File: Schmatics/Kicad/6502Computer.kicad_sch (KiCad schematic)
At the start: 8 parts

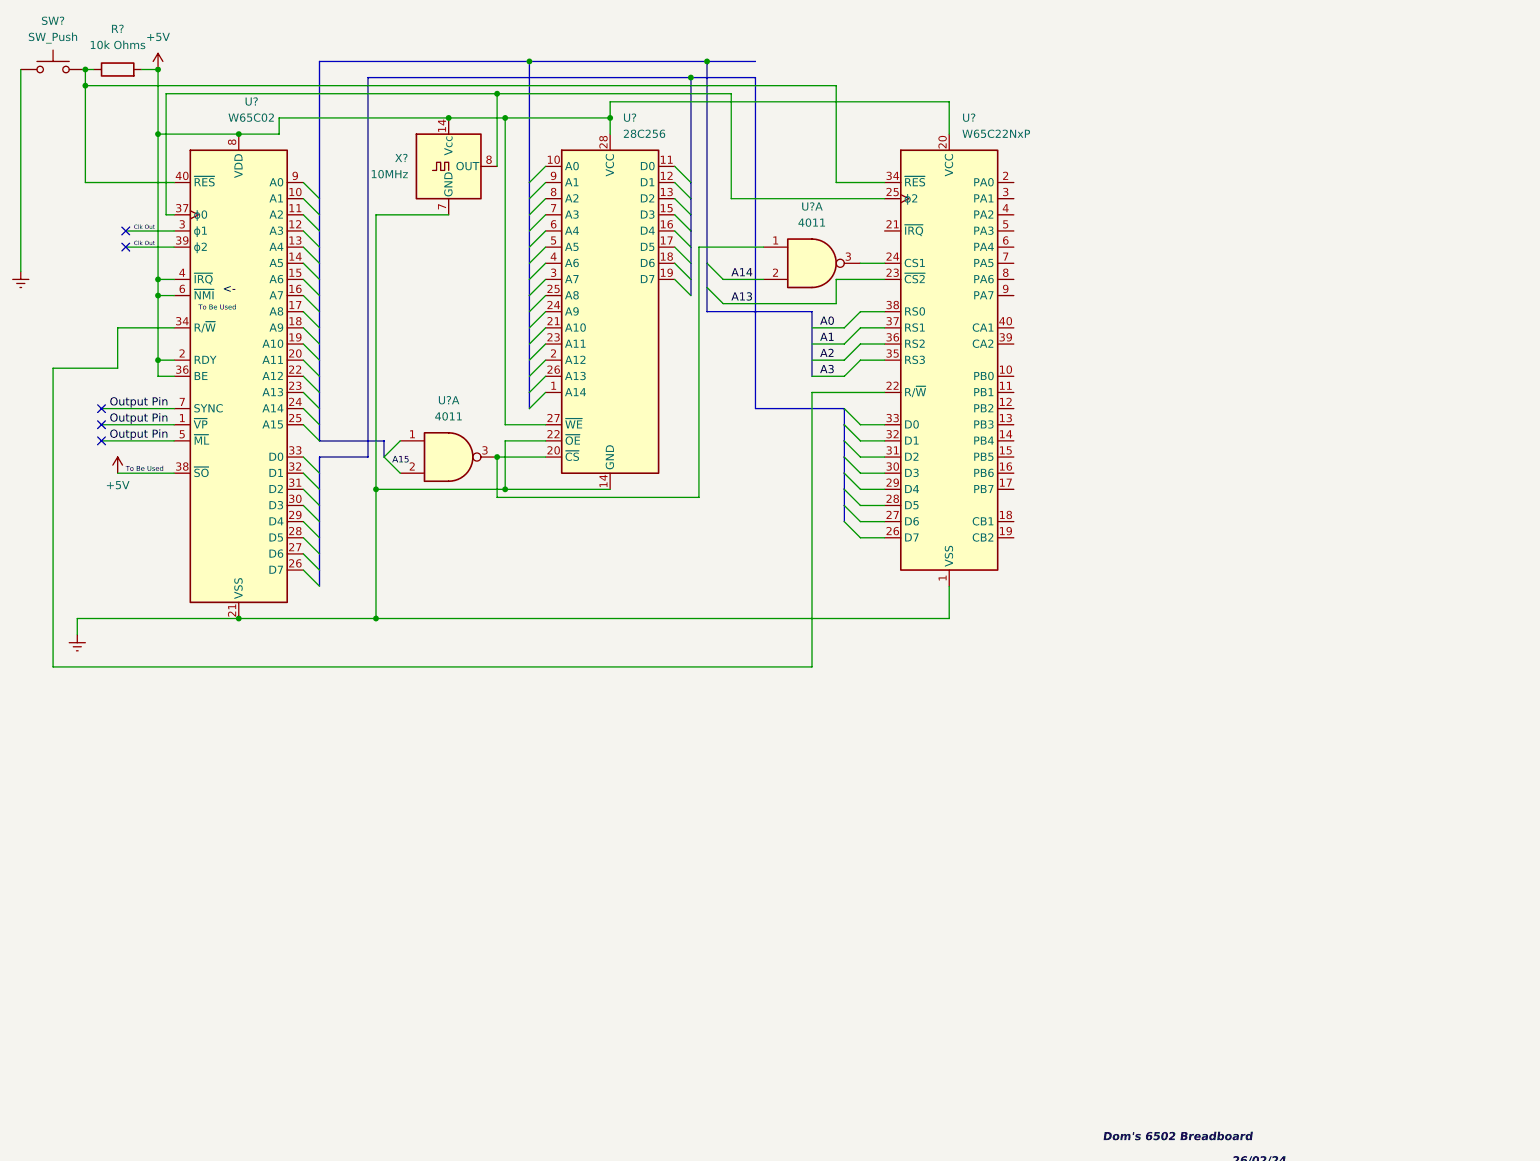
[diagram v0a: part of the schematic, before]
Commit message: Update schematic configuration and add new components
The schematic configuration was updated to include presets and detailed design settings. Two new elements, a trim-potentiometer and an LCD display, were also added to the PSI schematic. In addition, information about a new RAM memory HM62256BLP was added.
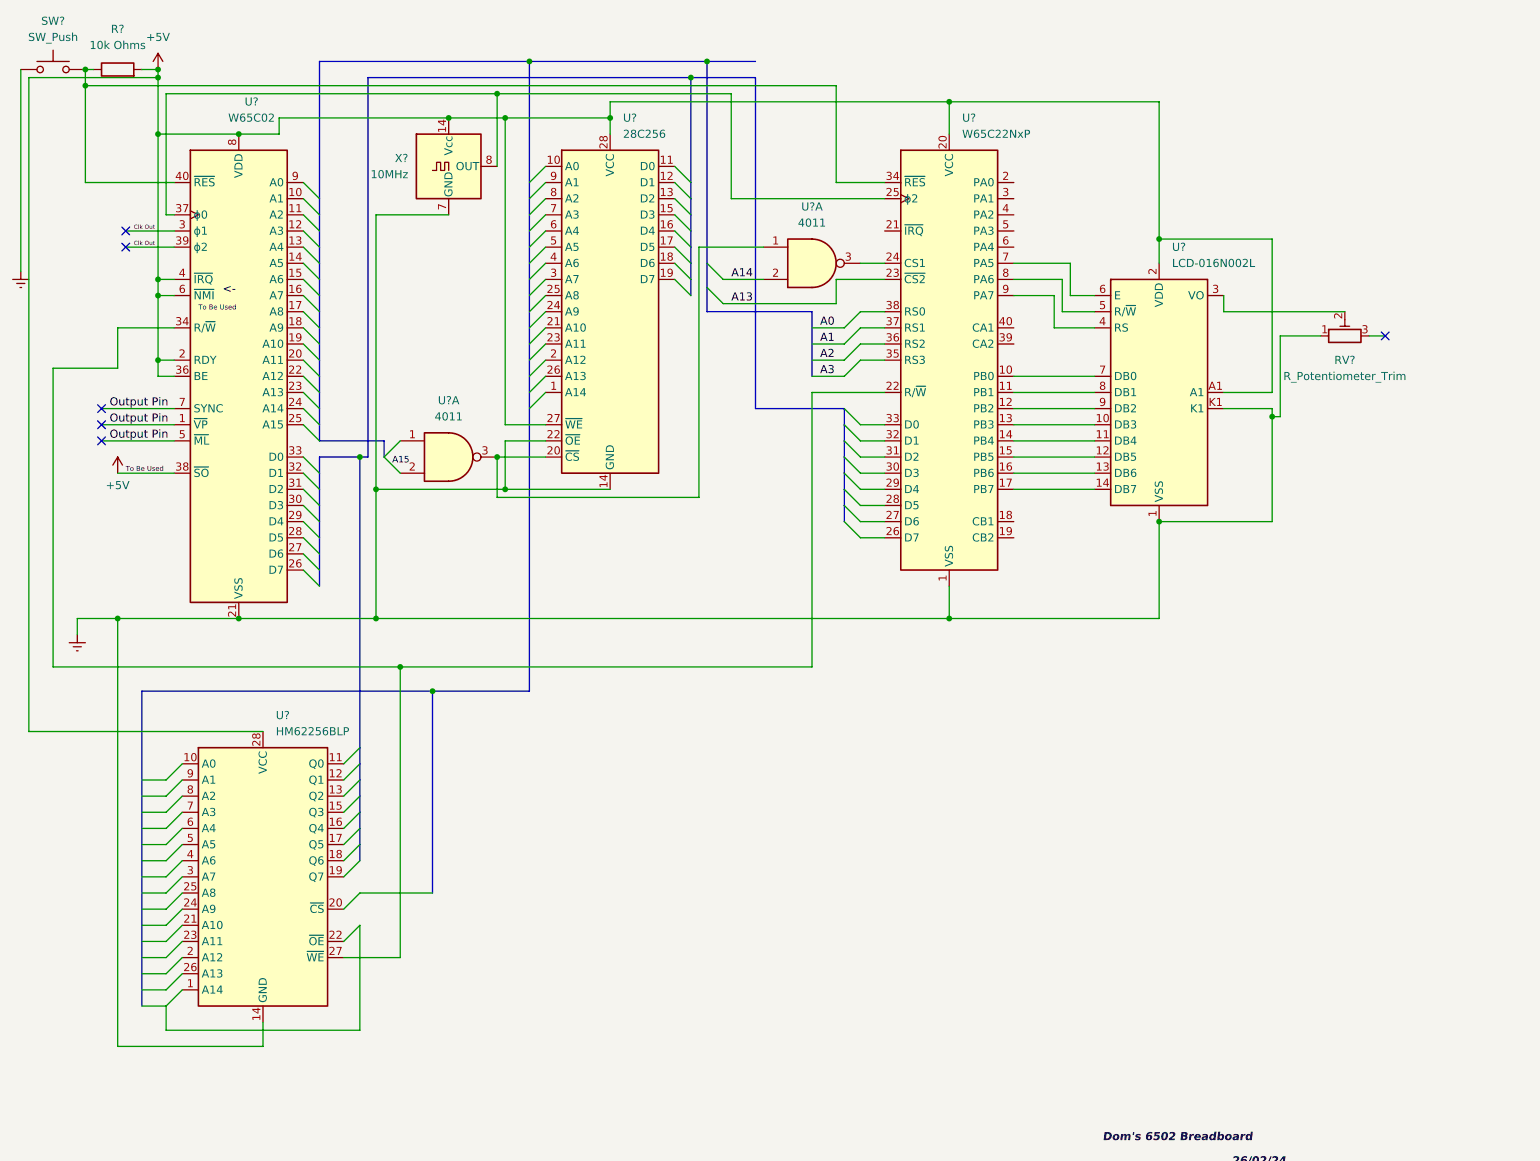
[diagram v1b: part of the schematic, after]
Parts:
- added RV?: R_Potentiometer_Trim, symbol Device:R_Potentiometer_Trim
- added U?: LCD-016N002L, Display:LCD-016N002L, symbol Display_Character:LCD-016N002L
- added U?: HM62256BLP, Package_DIP:DIP-28_W15.24mm, symbol Memory_RAM:HM62256BLP
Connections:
- net +5V: now also U?.2 (VDD), U?.28 (VCC), U?.A1
- net Earth: now also RV?.1, U?.1 (VSS), U?.14 (GND), U?.K1
- net at U?.10 (PB0): now also U?.7 (DB0)
- net at U?.11 (PB1): now also U?.8 (DB1)
- net at U?.12 (PB2): now also U?.9 (DB2)
- net at U?.13 (PB3): now also U?.10 (DB3)
- net at U?.14 (PB4): now also U?.11 (DB4)
- net at U?.15 (PB5): now also U?.12 (DB5)
- net at U?.16 (PB6): now also U?.13 (DB6)
- net at U?.17 (PB7): now also U?.14 (DB7)
- net at U?.22 (R/~{W}), U?.34 (R/~{W}): now also U?.27 (~{WE})
- net at U?.7 (PA5): now also U?.6 (E)
- net at U?.8 (PA6): now also U?.5 (R/~{W})
- net at U?.9 (PA7): now also U?.4 (RS)
- new net: RV?.2, U?.3 (VO)
- no-connect marks 5 -> 6

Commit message: Schemat
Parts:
- added C1, C2: 22pF, symbol Device:C
- added J1: Video Out, symbol Connector:Conn_Coaxial
- added R1: 470R, symbol Device:R
- added R2: 1K, symbol Device:R
- added R3: 10K, symbol Device:R
- added U1: 74HCT166, symbol 74xx:74HCT164
- added U2: ATmega328-P, Package_DIP:DIP-28_W7.62mm, symbol MCU_Microchip_ATmega:ATmega328-P
- added Y1: Crystal, symbol Device:Crystal
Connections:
- net A14 is gone; now on net A13: U?.2
- net +5V: now also U1.16 (VCC)
- net A13: now also R?.1, SW?.2, U?.34 (~{RES}), U?.40 (~{RES}), U1.9 (~{MR})
- net Earth: now also J1.2 (Ext), R3.2, U1.1 (DS), U1.6 (CE), U1.8 (GND), U2.20 (AVCC), U2.22 (GND), U2.7 (VCC), U2.8 (GND)
- new net: C1.1, U2.9 (XTAL1/PB6), Y1.2
- new net: C1.2, C2.2
- new net: R2.1, U2.14 (PB0)
- new net: J1.1 (In), R1.2, R2.2
- new net: C2.1, U1.7 (CP), U2.10 (XTAL2/PB7), Y1.1
- new net: R1.1, U1.13 (Q7)
- new net: U1.15 (PEB), U2.26 (PC3)
- new net PD7: R3.1

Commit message: Schemat
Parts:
- removed R?: 10k Ohms, symbol Device:R
- removed RV?: R_Potentiometer_Trim, symbol Device:R_Potentiometer_Trim
- removed U? (x2): 4011, symbol 4xxx:4011
- removed U?: W65C22NxP, Package_DIP:DIP-40_W15.24mm, symbol 6502:W65C22NxP
- removed U?: 28C256, symbol EEProm:28C256
- removed U?: LCD-016N002L, Display:LCD-016N002L, symbol Display_Character:LCD-016N002L
- removed U?: HM62256BLP, Package_DIP:DIP-28_W15.24mm, symbol Memory_RAM:HM62256BLP
- removed U?: W65C02, Package_DIP:DIP-40_W15.24mm, symbol 6502:W65C02SxP
- removed X?: 10MHz, Oscillator:Oscillator_DIP-14, symbol Oscillator:ACO-xxxMHz
- added C3, C4: 22pF, symbol Device:C
- added C5, C6, C7, C8: 0.1uf, symbol Device:C
- added J2: Keyboard + Video, symbol Connector:DE9_Plug
- added J3: PS/2 Keyboard, symbol Connector:Mini-DIN-6
- added R4, R5: 10K, symbol Device:R
- added R6, R7: 4K7, symbol Device:R
- added R8: 10k Ohms, symbol Device:R
- added RV1: R_Potentiometer_Trim, symbol Device:R_Potentiometer_Trim
- added U10: HM62256BLP, Package_DIP:DIP-28_W15.24mm, symbol Memory_RAM:HM62256BLP
- added U3: ATmega88-20P, Package_DIP:DIP-28_W7.62mm, symbol MCU_Microchip_ATmega:ATmega88-20P
- added U4: W65C02, Package_DIP:DIP-40_W15.24mm, symbol 6502:W65C02SxP
- added U5, U7: 4011, symbol 4xxx:4011
- added U6: 28C256, symbol EEProm:28C256
- added U8: W65C22NxP, Package_DIP:DIP-40_W15.24mm, symbol 6502:W65C22NxP
- added U9: LCD-016N002L, Display:LCD-016N002L, symbol Display_Character:LCD-016N002L
- added X1: 10MHz, Oscillator:Oscillator_DIP-14, symbol Oscillator:ACO-xxxMHz
- added Y2: 11.0592Mhz, symbol Device:Crystal
- J1: value Video Out -> Video Out RCA
- gave numbers to parts that had none: 1
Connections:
- net +5V: now also C5.1, C6.1, C7.1, C8.1, J3.4, R4.1, R5.1, R8.2, U10.28 (VCC), U3.20 (AVCC), U3.7 (VCC), U4.2 (RDY), U4.36 (BE), U4.38 (~{SO}), U4.4 (~{IRQ}), U4.6 (~{NMI}), U4.8 (VDD), U6.27 (~{WE}), U6.28 (VCC), U8.20 (VCC), U9.2 (VDD), U9.A1, X1.14 (Vcc)
- net A13: now also U2.1 (~{RESET}/PC6), R8.1, U3.1 (~{RESET}/PC6), U4.40 (~{RES}), U7.2, U8.23 (~{CS2}), U8.34 (~{RES})
- net Clk Out: now also U4.3 (ϕ1), U4.39 (ϕ2)
- net Earth: now also C3.2, C4.2, C5.2, C6.2, C7.2, C8.2, J2.5, J3.3, R6.1, R7.1, RV1.1, U10.14 (GND), U3.22 (GND), U3.8 (GND), U4.21 (VSS), U6.14 (GND), U6.22 (~{OE}), U8.1 (VSS), U9.1 (VSS), U9.K1, X1.7 (GND)
- net Output Pin: now also U4.1 (~{VP}), U4.5 (~{ML}), U4.7 (SYNC)
- net at U1.15 (PEB), U2.26 (PC3): now also R7.2
- net at U2.15 (PB1): now also U3.14 (PB0)
- net at U2.16 (PB2): now also U3.13 (PD7)
- net at U2.17 (PB3): now also U3.12 (PD6)
- net at U2.18 (PB4): now also U3.11 (PD5)
- net at U2.19 (PB5): now also U3.19 (PB5)
- net at U2.23 (PC0): now also U3.6 (PD4)
- net at U2.24 (PC1): now also U3.5 (PD3)
- net at U2.25 (PC2): now also U3.4 (PD2)
- net at U2.27 (PC4): now also R6.2, U3.27 (PC4)
- net at U2.28 (PC5): now also U3.28 (PC5)
- new net: U4.37 (ϕ0), U8.25 (ϕ2), X1.8 (OUT)
- new net: U5.3, U6.20 (~{CS}), U7.1
- new net: U7.3, U8.24 (CS1)
- new net: J3.1, R4.2, U3.25 (PC2)
- new net: J3.5, R5.2, U3.24 (PC1)
- new net: U8.10 (PB0), U9.7 (DB0)
- new net: U8.11 (PB1), U9.8 (DB1)
- new net: U8.12 (PB2), U9.9 (DB2)
- new net: U8.13 (PB3), U9.10 (DB3)
- new net: U8.14 (PB4), U9.11 (DB4)
- new net: U8.15 (PB5), U9.12 (DB5)
- new net: U8.16 (PB6), U9.13 (DB6)
- new net: U8.17 (PB7), U9.14 (DB7)
- new net: U10.27 (~{WE}), U4.34 (R/~{W}), U8.22 (R/~{W})
- new net: U8.7 (PA5), U9.6 (E)
- new net: U8.8 (PA6), U9.5 (R/~{W})
- new net: U8.9 (PA7), U9.4 (RS)
- new net: C4.1, U3.9 (XTAL1/PB6), Y2.1
- new net: C3.1, U3.10 (XTAL2/PB7), Y2.2
- new net: J2.2, U3.2 (PD0)
- new net: J2.7, U3.26 (PC3)
- new net: J2.3, U3.3 (PD1)
- new net: RV1.2, U9.3 (VO)
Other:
- moved on the sheet: J1

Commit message: Add new power symbols, a resistor and a NPN transistor to KiCad schematic
In this commit, new "+5V", "Earth" power symbols and a "NPN" transistor were added into the "6502Computer.kicad_sch" KiCad schematic for realistic power simulation. A 10k resistor ("R9") has also been included. These additions will provide more granularity and accuracy in the upcoming circuit simulations.
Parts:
- added Q1: NPN, symbol Simulation_SPICE:NPN
- added R9: 10k, symbol Device:R
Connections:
- net +5V: now also R9.1
- net Earth: now also Q1.3 (E)
- new net: Q1.1 (C), R9.2
- no-connect marks 6 -> 8

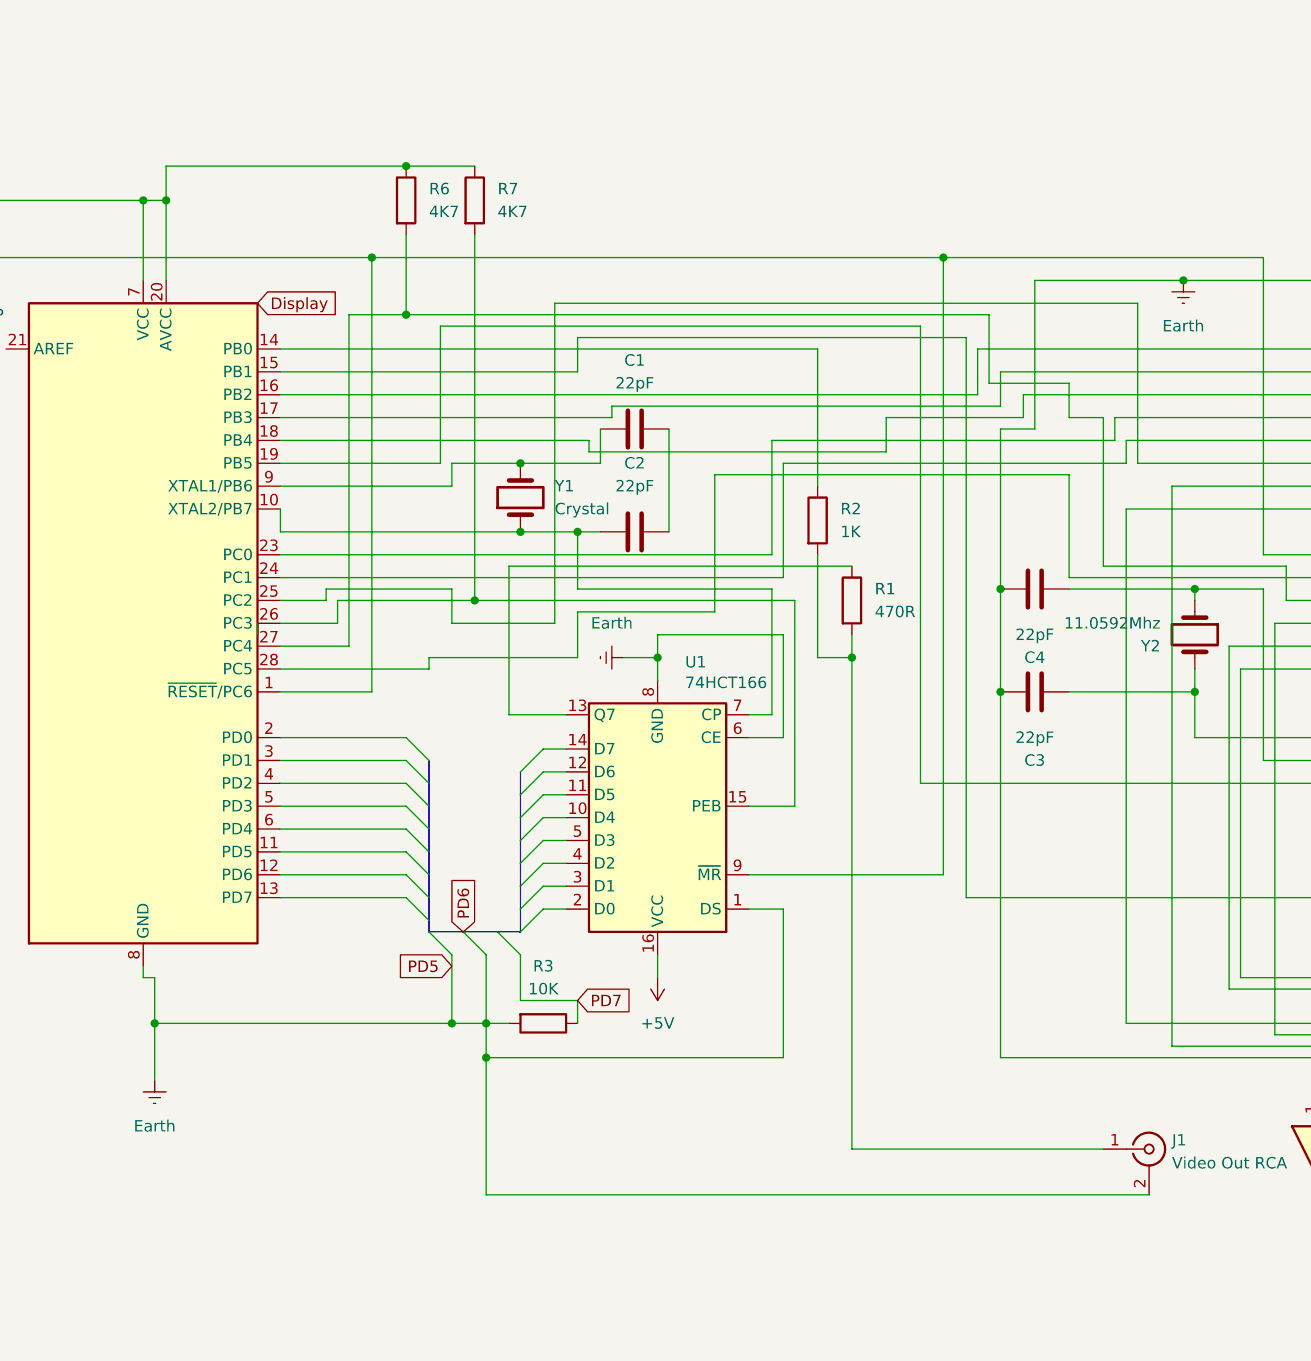
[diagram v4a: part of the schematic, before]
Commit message: Add switch to schematic and update makefile
This commit introduces a Single Pole Single Throw (SPST) switch to Kicad schematic and adjust wire connections accordingly. The Makefile is also updated to include 'WriteChip' command for writing binary files to a chip. These changes pave the way for further hardware control and manipulation.
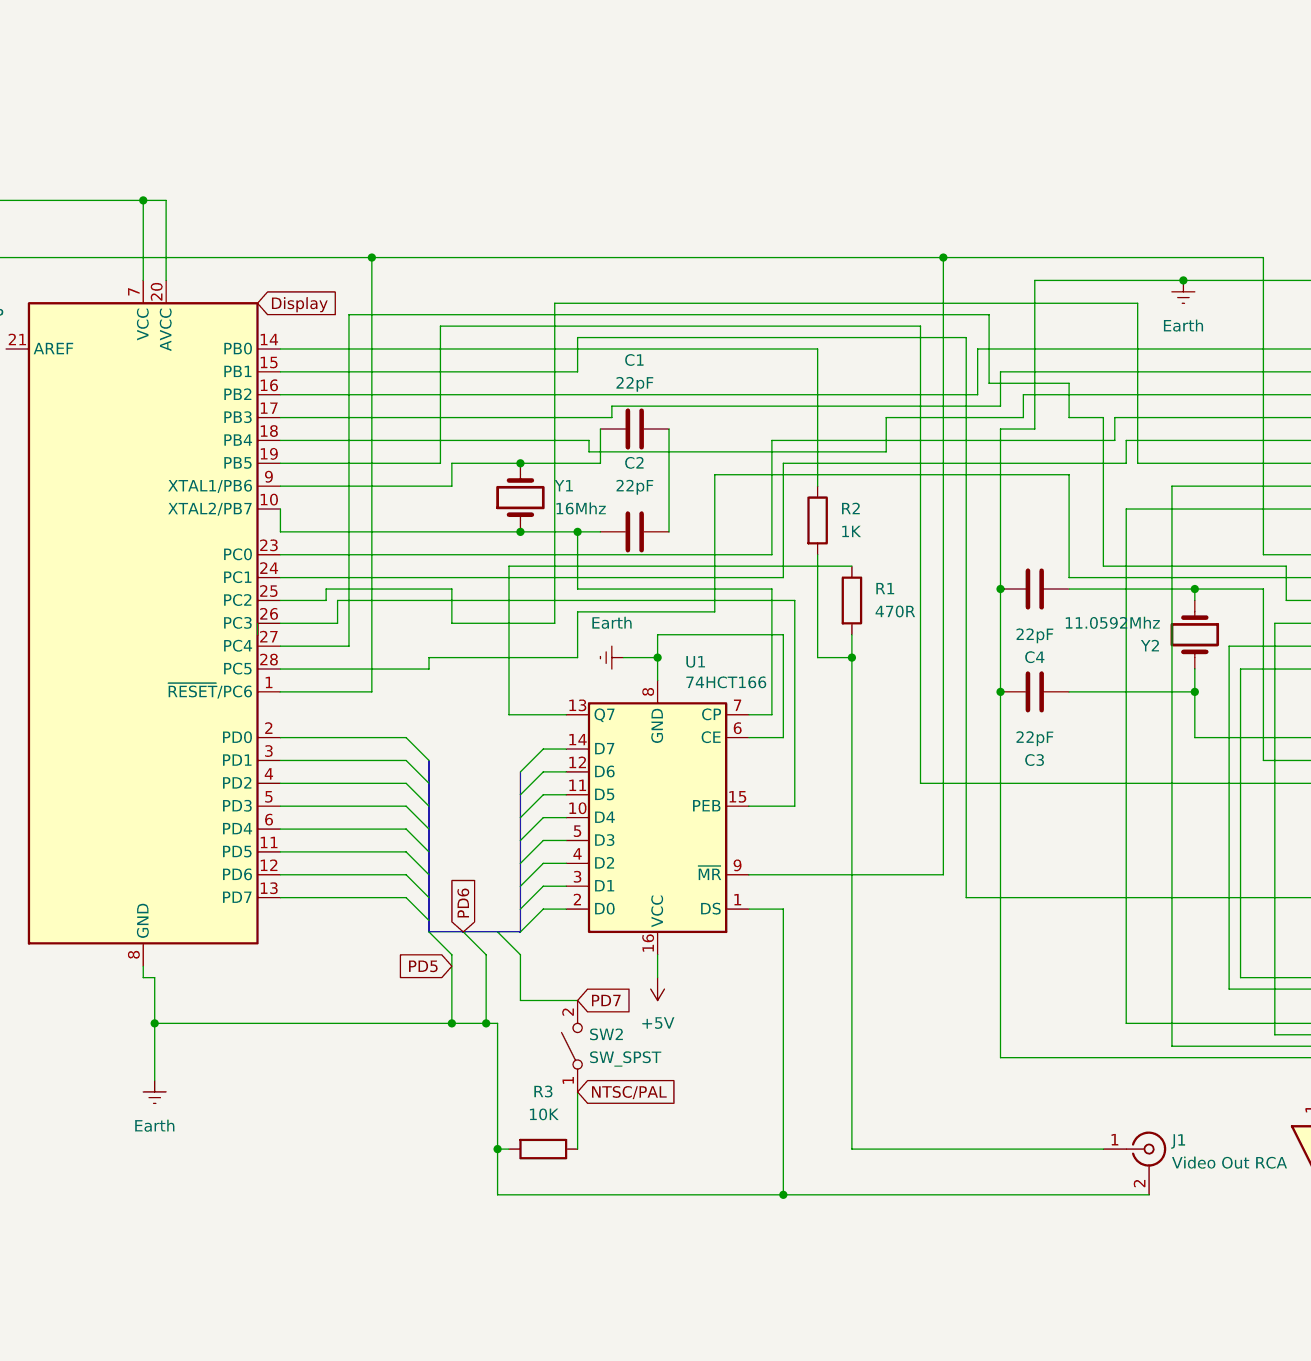
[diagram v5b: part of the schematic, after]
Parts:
- removed R6, R7: 4K7, symbol Device:R
- added SW2: SW_SPST, symbol Switch:SW_SPST
- Y1: value Crystal -> 16Mhz
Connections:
- net PD7: now also SW2.2 (B); no longer R3.1
- new net NTSC/PAL: R3.1, SW2.1 (A)
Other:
- moved on the sheet: R3
